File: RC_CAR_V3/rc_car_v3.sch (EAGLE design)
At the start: 45 parts, among them IC1 LIS2DW12TR, IC3 VNH7070BASTR, IC4 BQ34110PWR, J1 282836-2, J2 282836-2, J3 282836-2, Q2 SI2333DDS-T1-GE3, Q3 2N7002-7-F, U1 MCP1703T-3302E/DB

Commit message: PCB
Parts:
- removed IC3: VNH7070BASTR, SamacSys_Parts:VNH7070BASTR
- removed PSOC1: PSOC_5LP, PSoC 5LP:PSOC_5LP
- removed Q3: 2N7002-7-F, SamacSys_Parts:2N7002-7-F
- added C16: 68000-404HLF, SamacSys_Parts:68000-404HLF
- added C17, C18, C19, C20, C21, C22, C23, C24: 0.1uF, SamacSys_Parts:C0603C104K5RAC3121
- added IC2: INA199B3DCKR, SamacSys_Parts:INA199B3DCKR
- added J4: 282836-2, 282836-2:282836-2
- added Q1: 2N7002-7-F, SamacSys_Parts:2N7002-7-F
- added Q5: SQJ912AEP-T2_BE3, SamacSys_Parts:SQJ912AEP-T2_BE3
- added Q7: SI7923DN-T1-E3, SamacSys_Parts:SI7923DN-T1-E3
- C3: value C0603C104K5RAC3121 -> 10uF
- IC4: value BQ34110PWR -> CY8C5888LTI-LP097; device SamacSys_Parts:BQ34110PWR -> SamacSys_Parts:CY8C5888LTI-LP097
- J3: value 282836-2 -> 1-1734742-8; device 282836-2:282836-2 -> SamacSys_Parts:1-1734742-8
- Q2: value SI2333DDS-T1-GE3 -> 2N7002-7-F; device SI2333DDS-T1-GE3:SI2333DDS-T1-GE3 -> SamacSys_Parts:2N7002-7-F
- R10: value ERA-3AED304V -> ERJ-D2DFR022V; device SamacSys_Parts:ERA-3AED304V -> SamacSys_Parts:ERJ-D2DFR022V
- R2, R4: value ERJ-UP3F1000V -> 1k
- R7: value ERJ-3RBD4302V -> 1k; device SamacSys_Parts:ERJ-3RBD4302V -> SamacSys_Parts:ERJ-UP3F1000V
- R8, R9: value ERA-3AED304V -> 1k; device SamacSys_Parts:ERA-3AED304V -> SamacSys_Parts:ERJ-UP3F1000V
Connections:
- removed net BAT: IC4.BAT, R7.2, R8.1
- removed net DIST_1: PSOC1.2.3
- removed net DIST_2: PSOC1.2.2
- removed net DIST_3: PSOC1.2.0
- removed net MOTOR_CURRENT: IC3.CS, R16.1
- removed net N$11: IC3.INB, R15.1
- removed net N$5: C3.1, IC4.REG25
- removed net N$6: Q2.D, R8.2
- removed net N$8: Q2.G, Q3.D, R10.1
- removed net OUTA: IC3.OUTA_1, J3.1
- removed net OUTB: IC3.OUTB_1, J3.2
- removed net PWM: IC3.PWM, R14.2
- removed net PWM1: PSOC1.0.6, R16.2
- removed net SRP: J1.2, R1.1, R4.2
- removed net VEN: IC4.VEN/GPIO, Q3.G
- new net D1: J4.1, Q5.D1_1, Q5.D1_2, Q5.D1_3, Q7.D1_1, Q7.D1_2
- new net D2: J4.2, Q5.D2_1, Q5.D2_2, Q5.D2_3, Q7.D2_1, Q7.D2_2
- new net FWD: Q1.D, Q7.G2, R14.1
- new net IMOTOR: C24.1, IC4.P0[3]_(GPIO,_OPAMP0-,_EXTREF0), R9.1
- new net ISENSE: IC2.OUT, IC4.(OPAMP3-,_EXTREF1,_GPIO)_P3[2]
- new net N$16: C21.2, IC4.(NTRST,_GPIO)_P1[5]
- new net N$21: J3.6, J3.8
- new net RVRS: Q2.D, Q7.G1, R13.1
- new net SRC: Q5.S1, Q5.S2, R10.2, R9.2
- new net SWDCK: IC4.(TCK,_SWDCK,_GPIO)_P1[1], J3.2
- new net SWDIO: IC4.(TMS,_SWDIO,_GPIO)_P1[0], J3.3
- new net VBAT: C3.1, IC4.(OPAMP1+,_GPIO)_P3[5], R2.2, R7.1
- new net XRES: IC4.!XRES, J3.4
- net 0: now also C16.3, C16.4, C17.1, C18.2, C19.1, C20.1, C21.1, C22.2, C23.2, C24.2, IC2.GND, IC2.REF, IC4.EP, IC4.VBAT, IC4.VBOOST, IC4.VSSB, IC4.VSSD_1, IC4.VSSD_2, J1.2, J2.2, Q1.S, Q2.S, R10.1, R2.1; no longer IC3.GNDA_1, IC3.GNDA_2, IC3.GNDB_2, IC4.VSS, PSOC1.GND, PSOC1.GND_3, Q3.S, R1.2, R2.2, R7.1
- net 3.3V: now also IC2.V+, R4.2, R8.2; no longer IC4.REGIN, R3.2, R5.2
- net CTS: now also IC4.(I2C0:_SCL,_SIO)_P12[4]; no longer PSOC1.12.4
- net CTS_JETSON: now also IC4.VDDIO0; no longer PSOC1.2.7
- net ECHO_1: now also IC4.P2[3]_(GPIO,_TRACECLK)
- net ECHO_2: now also IC4.P2[2]_(GPIO)
- net ECHO_3: now also IC4.P2[0]_(GPIO)
- net FORWARD: now also IC4.P0[1]_(GPIO,_OPAMP0OUT), R15.2, R3.2; no longer PSOC1.1.7, R13.2
- net N$10: now also C17.2, C18.1, IC4.VCCD_1, IC4.VCCD_2; no longer IC3.INA, R13.1
- net N$13: now also Q1.G, R16.1; no longer J2.2
- net N$2: now also Q5.G1, R3.1; no longer R10.2, R9.1
- net N$3: now also IC2.IN+, J1.1, R1.1; no longer IC4.SRN, R2.1
- net N$4: now also Q2.G, R15.1; no longer IC4.SRP, R4.1
- net N$7: now also Q5.G2, R5.1; no longer PSOC1.1.6, R14.1
- net REVERSE: now also IC4.P0[7]_(GPIO,_IDAC2), R16.2, R5.2; no longer PSOC1.0.7, R15.2
- net RTS: now also IC4.(I2C0:_SDA,_SIO)_P12[5]; no longer PSOC1.12.5
- net RTS_JETSON: now also IC4.P0[5]_(GPIO,_OPAMP2-); no longer PSOC1.2.6
- net RX: now also IC4.(SIO)_P12[6]; no longer PSOC1.12.2
- net RX_JETSON: now also IC4.P12[3]_(SIO); no longer PSOC1.12.6
- net SCL: now also IC4.P12[0]_(SIO,_12C1:_SCL), R8.1; no longer IC4.SCL, PSOC1.12.0_SCL, R3.1
- net SDA: now also IC4.P12[1]_(SIO,_I2C1:_SDA), R4.1; no longer IC4.SDA, PSOC1.12.1_SDA, R5.1
- net SERVO: now also C16.2, IC4.P2[5]_(GPIO,_TRACEDATA[1]); no longer PSOC1.2.5
- net SPEED: now also IC4.P15[4]_(GPIO); no longer PSOC1.15.4
- net TRIG: now also IC4.P2[4]_(GPIO,_TRACEDATA[0]); no longer PSOC1.2.4
- net TX: now also IC4.(SIO)_P12[7]; no longer PSOC1.12.3
- net TX_JETSON: now also IC4.P12[2]_(SIO); no longer PSOC1.12.7
- net VBUS: now also C16.1, IC2.IN-, Q7.S1, Q7.S2, R1.2, R13.2, R14.2, R7.2; no longer IC3.VCC_1, IC3.VCC_2, IC3.VCC_3, J1.1, Q2.S, R9.2
- net VDD: now also C19.2, C20.2, C22.1, C23.1, IC4.VDDD_1, IC4.VDDD_2, IC4.VDDIO1, IC4.VDDIO2, IC4.VDDIO3; no longer PSOC1.VDD, PSOC1.VDD_2
- net VSENSE: now also IC4.(OPAMP1-,_GPIO)_P3[4]
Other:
- moved on the sheet: C3, R1, R10

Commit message: Added more connections
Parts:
- added C25, C26: 0.1uF, SamacSys_Parts:C0603C104K5RAC3121
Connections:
- new net N$6: C25.2, IC4.VCCA
- net 0: now also C25.1, C26.1, IC4.VSSA, IC4.VSSD_3
- net VDD: now also C26.2, IC4.VDDA
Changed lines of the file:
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@@
 <?xml version="1.0" encoding="utf-8"?>
 <!DOCTYPE eagle SYSTEM "eagle.dtd">
-<eagle version="9.6.2">
+<eagle version="9.3.2">
 <drawing>
 <settings>
@@
 <part name="C24" library="SamacSys_Parts" deviceset="C0603C104K5RAC3121" device="" value="0.1uF"/>
 <part name="X_39" library="ngspice-simulation" library_urn="urn:adsk.eagle:library:527439" deviceset="GND" device=""/>
+<part name="X_40" library="ngspice-simulation" library_urn="urn:adsk.eagle:library:527439" deviceset="GND" device=""/>
+<part name="C25" library="SamacSys_Parts" deviceset="C0603C104K5RAC3121" device="" value="0.1uF"/>
+<part name="X_41" library="ngspice-simulation" library_urn="urn:adsk.eagle:library:527439" deviceset="GND" device=""/>
+<part name="C26" library="SamacSys_Parts" deviceset="C0603C104K5RAC3121" device="" value="0.1uF"/>
+<part name="X_42" library="ngspice-simulation" library_urn="urn:adsk.eagle:library:527439" deviceset="GND" device=""/>
 </parts>
 <sheets>
@@
 <attribute name="VALUE" x="105.41" y="-25.4" size="1.778" layer="96" align="center-left"/>
 </instance>
-<instance part="R4" gate="G$1" x="147.32" y="-106.68" smashed="yes" rot="R90"/>
-<instance part="R8" gate="G$1" x="157.48" y="-106.68" smashed="yes" rot="R90"/>
+<instance part="R4" gate="G$1" x="162.56" y="-106.68" smashed="yes" rot="R90"/>
+<instance part="R8" gate="G$1" x="172.72" y="-106.68" smashed="yes" rot="R90"/>
 <instance part="J4" gate="G$1" x="411.48" y="-162.56" smashed="yes" rot="MR0">
 <attribute name="NAME" x="412.752359375" y="-156.707159375" size="1.017890625" layer="95" rot="MR0"/>
@@
 </instance>
 <instance part="X_39" gate="G$1" x="353.06" y="-203.2" smashed="yes"/>
+<instance part="X_40" gate="G$1" x="134.62" y="-91.44" smashed="yes" rot="R90"/>
+<instance part="C25" gate="G$1" x="132.08" y="-99.06" smashed="yes" rot="R180">
+<attribute name="NAME" x="128.27" y="-102.87" size="1.778" layer="95" rot="R180" align="center-left"/>
+<attribute name="VALUE" x="128.27" y="-95.25" size="1.778" layer="96" rot="R180" align="center-left"/>
+</instance>
+<instance part="X_41" gate="G$1" x="134.62" y="-99.06" smashed="yes" rot="R90"/>
+<instance part="C26" gate="G$1" x="149.86" y="-96.52" smashed="yes" rot="R90">
+<attribute name="NAME" x="146.05" y="-92.71" size="1.778" layer="95" rot="R90" align="center-left"/>
+<attribute name="VALUE" x="153.67" y="-92.71" size="1.778" layer="96" rot="R90" align="center-left"/>
+</instance>
+<instance part="X_42" gate="G$1" x="149.86" y="-99.06" smashed="yes"/>
 </instances>
 <busses>
@@
 </segment>
 <segment>
-<wire x1="147.32" y1="-88.9" x2="147.32" y2="-81.28" width="0.1524" layer="91"/>
-<wire x1="147.32" y1="-81.28" x2="157.48" y2="-81.28" width="0.1524" layer="91"/>
-<wire x1="157.48" y1="-81.28" x2="157.48" y2="-88.9" width="0.1524" layer="91"/>
-<label x="152.4" y="-78.74" size="1.778" layer="95"/>
+<wire x1="162.56" y1="-88.9" x2="162.56" y2="-81.28" width="0.1524" layer="91"/>
+<wire x1="162.56" y1="-81.28" x2="172.72" y2="-81.28" width="0.1524" layer="91"/>
+<wire x1="172.72" y1="-81.28" x2="172.72" y2="-88.9" width="0.1524" layer="91"/>
+<label x="167.64" y="-78.74" size="1.778" layer="95"/>
 <pinref part="R4" gate="G$1" pin="2"/>
 <pinref part="R8" gate="G$1" pin="2"/>
@@
 <pinref part="X_39" gate="G$1" pin="0"/>
 </segment>
+<segment>
+<pinref part="X_40" gate="G$1" pin="0"/>
+<pinref part="IC4" gate="G$1" pin="VSSD_3"/>
+<wire x1="134.62" y1="-91.44" x2="119.38" y2="-91.44" width="0.1524" layer="91"/>
+<pinref part="IC4" gate="G$1" pin="VSSA"/>
+<wire x1="119.38" y1="-91.44" x2="109.22" y2="-91.44" width="0.1524" layer="91"/>
+<wire x1="109.22" y1="-96.52" x2="119.38" y2="-96.52" width="0.1524" layer="91"/>
+<wire x1="119.38" y1="-96.52" x2="119.38" y2="-91.44" width="0.1524" layer="91"/>
+<junction x="119.38" y="-91.44"/>
+</segment>
+<segment>
+<pinref part="C25" gate="G$1" pin="1"/>
+<pinref part="X_41" gate="G$1" pin="0"/>
+<wire x1="132.08" y1="-99.06" x2="134.62" y2="-99.06" width="0.1524" layer="91"/>
+</segment>
+<segment>
+<pinref part="C26" gate="G$1" pin="1"/>
+<pinref part="X_42" gate="G$1" pin="0"/>
+<wire x1="149.86" y1="-96.52" x2="149.86" y2="-99.06" width="0.1524" layer="91"/>
+</segment>
 </net>
 <net name="SCL" class="0">
@@
 <pinref part="IC4" gate="G$1" pin="P12[0]_(SIO,_12C1:_SCL)"/>
 <pinref part="R8" gate="G$1" pin="1"/>
-<wire x1="109.22" y1="-109.22" x2="157.48" y2="-109.22" width="0.1524" layer="91"/>
-<wire x1="157.48" y1="-109.22" x2="157.48" y2="-106.68" width="0.1524" layer="91"/>
-<label x="160.02" y="-109.22" size="1.778" layer="95"/>
+<wire x1="109.22" y1="-109.22" x2="172.72" y2="-109.22" width="0.1524" layer="91"/>
+<wire x1="172.72" y1="-109.22" x2="172.72" y2="-106.68" width="0.1524" layer="91"/>
+<label x="175.26" y="-109.22" size="1.778" layer="95"/>
 </segment>
 </net>
@@
 <pinref part="R4" gate="G$1" pin="1"/>
 <pinref part="IC4" gate="G$1" pin="P12[1]_(SIO,_I2C1:_SDA)"/>
-<wire x1="147.32" y1="-106.68" x2="109.22" y2="-106.68" width="0.1524" layer="91"/>
+<wire x1="162.56" y1="-106.68" x2="109.22" y2="-106.68" width="0.1524" layer="91"/>
 <label x="139.7" y="-104.14" size="1.778" layer="95"/>
 </segment>
@@
 <junction x="7.62" y="-167.64"/>
 </segment>
+<segment>
+<pinref part="IC4" gate="G$1" pin="VDDA"/>
+<wire x1="109.22" y1="-93.98" x2="142.24" y2="-93.98" width="0.1524" layer="91"/>
+<wire x1="142.24" y1="-93.98" x2="142.24" y2="-83.82" width="0.1524" layer="91"/>
+<pinref part="C26" gate="G$1" pin="2"/>
+<wire x1="142.24" y1="-83.82" x2="149.86" y2="-83.82" width="0.1524" layer="91"/>
+<label x="142.24" y="-83.82" size="1.778" layer="95"/>
+</segment>
 </net>
 <net name="N$9" class="0">
@@
 </segment>
 </net>
+<net name="N$6" class="0">
+<segment>
+<pinref part="C25" gate="G$1" pin="2"/>
+<wire x1="119.38" y1="-99.06" x2="109.22" y2="-99.06" width="0.1524" layer="91"/>
+<pinref part="IC4" gate="G$1" pin="VCCA"/>
+</segment>
+</net>

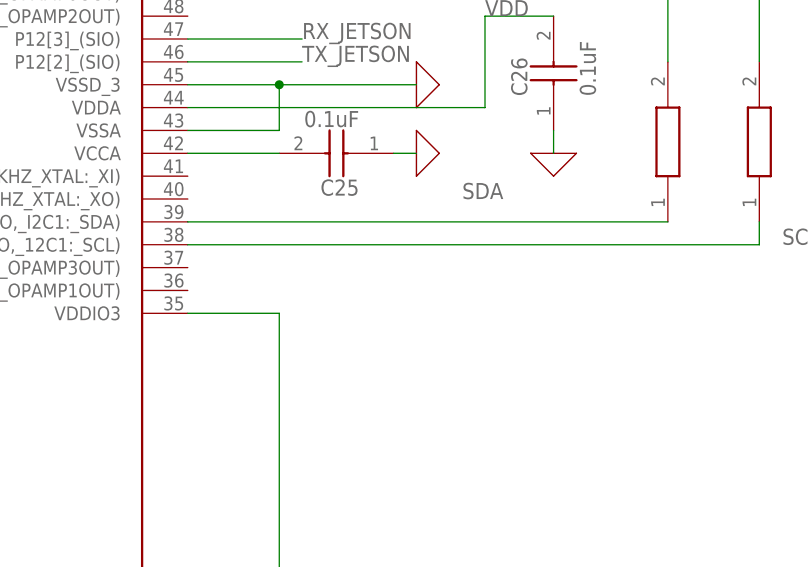
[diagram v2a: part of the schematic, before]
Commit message: Added ground planes
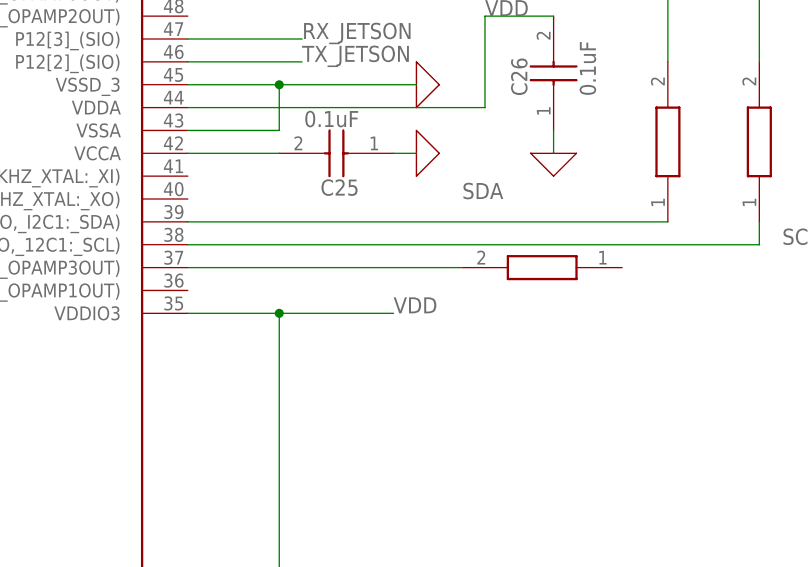
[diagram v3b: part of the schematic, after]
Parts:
- added R18: 1k, SamacSys_Parts:ERJ-UP3F1000V
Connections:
- new net N$5: IC4.P3[7]_(GPIO,_OPAMP3OUT), R18.2
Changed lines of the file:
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@@
 <?xml version="1.0" encoding="utf-8"?>
 <!DOCTYPE eagle SYSTEM "eagle.dtd">
-<eagle version="9.3.2">
+<eagle version="9.6.2">
 <drawing>
 <settings>
@@
 <part name="C26" library="SamacSys_Parts" deviceset="C0603C104K5RAC3121" device="" value="0.1uF"/>
 <part name="X_42" library="ngspice-simulation" library_urn="urn:adsk.eagle:library:527439" deviceset="GND" device=""/>
+<part name="R18" library="SamacSys_Parts" deviceset="ERJ-UP3F1000V" device="" value="1k"/>
 </parts>
 <sheets>
@@
 </instance>
 <instance part="X_42" gate="G$1" x="149.86" y="-99.06" smashed="yes"/>
+<instance part="R18" gate="G$1" x="157.48" y="-111.76" smashed="yes" rot="R180"/>
 </instances>
 <busses>
@@
 <wire x1="7.62" y1="-116.84" x2="7.62" y2="-167.64" width="0.1524" layer="91"/>
 <junction x="7.62" y="-167.64"/>
+<wire x1="119.38" y1="-116.84" x2="132.08" y2="-116.84" width="0.1524" layer="91"/>
+<junction x="119.38" y="-116.84"/>
+<label x="132.08" y="-116.84" size="1.778" layer="95"/>
 </segment>
 <segment>
@@
 </segment>
 </net>
+<net name="N$5" class="0">
+<segment>
+<pinref part="IC4" gate="G$1" pin="P3[7]_(GPIO,_OPAMP3OUT)"/>
+<wire x1="109.22" y1="-111.76" x2="139.7" y2="-111.76" width="0.1524" layer="91"/>
+<pinref part="R18" gate="G$1" pin="2"/>
+</segment>
+</net>
 </nets>
 </sheet>
 </sheets>
+<errors>
+</errors>
 </schematic>
 </drawing>

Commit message: Done
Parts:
- added LED1: LTST-C191TBKT, SamacSys_Parts:LTST-C191TBKT
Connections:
- removed net N$5: IC4.P3[7]_(GPIO,_OPAMP3OUT), R18.2
- new net LED: IC4.(IDAC1,_GPIO)_P3[0], R18.2
- new net N$8: LED1.K, R18.1
- net 5V: now also LED1.A
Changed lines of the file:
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@@
 <part name="X_42" library="ngspice-simulation" library_urn="urn:adsk.eagle:library:527439" deviceset="GND" device=""/>
 <part name="R18" library="SamacSys_Parts" deviceset="ERJ-UP3F1000V" device="" value="1k"/>
+<part name="LED1" library="SamacSys_Parts" deviceset="LTST-C191TBKT" device=""/>
 </parts>
 <sheets>
@@
 </instance>
 <instance part="X_42" gate="G$1" x="149.86" y="-99.06" smashed="yes"/>
-<instance part="R18" gate="G$1" x="157.48" y="-111.76" smashed="yes" rot="R180"/>
+<instance part="R18" gate="G$1" x="134.62" y="-198.12" smashed="yes" rot="R180"/>
+<instance part="LED1" gate="G$1" x="134.62" y="-203.2" smashed="yes" rot="R270">
+<attribute name="NAME" x="143.51" y="-215.9" size="1.778" layer="95" rot="R270"/>
+<attribute name="VALUE" x="140.97" y="-215.9" size="1.778" layer="96" rot="R270"/>
+</instance>
 </instances>
 <busses>
@@
 <wire x1="396.24" y1="-93.98" x2="391.16" y2="-93.98" width="0.1524" layer="91"/>
 <label x="373.38" y="-93.98" size="1.778" layer="95"/>
+</segment>
+<segment>
+<pinref part="LED1" gate="G$1" pin="A"/>
+<wire x1="134.62" y1="-218.44" x2="134.62" y2="-226.06" width="0.1524" layer="91"/>
+<label x="132.08" y="-228.6" size="1.778" layer="95"/>
 </segment>
 </net>
@@
 </segment>
 </net>
-<net name="N$5" class="0">
-<segment>
-<pinref part="IC4" gate="G$1" pin="P3[7]_(GPIO,_OPAMP3OUT)"/>
-<wire x1="109.22" y1="-111.76" x2="139.7" y2="-111.76" width="0.1524" layer="91"/>
+<net name="N$8" class="0">
+<segment>
+<pinref part="LED1" gate="G$1" pin="K"/>
+<pinref part="R18" gate="G$1" pin="1"/>
+<wire x1="134.62" y1="-203.2" x2="134.62" y2="-198.12" width="0.1524" layer="91"/>
+</segment>
+</net>
+<net name="LED" class="0">
+<segment>
 <pinref part="R18" gate="G$1" pin="2"/>
-</segment>
-</net>
+<wire x1="116.84" y1="-198.12" x2="106.68" y2="-198.12" width="0.1524" layer="91"/>
+<label x="101.6" y="-198.12" size="1.778" layer="95"/>
+</segment>
+<segment>
+<pinref part="IC4" gate="G$1" pin="(IDAC1,_GPIO)_P3[0]"/>
+<wire x1="66.04" y1="-165.1" x2="66.04" y2="-172.72" width="0.1524" layer="91"/>
+<label x="66.04" y="-180.34" size="1.778" layer="95" rot="R90"/>
+</segment>
+</net>

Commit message: Cganges
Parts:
- removed Q1, Q2: 2N7002-7-F, SamacSys_Parts:2N7002-7-F
- removed Q5: SQJ912AEP-T2_BE3, SamacSys_Parts:SQJ912AEP-T2_BE3
- removed Q7: SI7923DN-T1-E3, SamacSys_Parts:SI7923DN-T1-E3
- removed R10: ERJ-D2DFR022V, SamacSys_Parts:ERJ-D2DFR022V
- removed R13, R14, R15, R16, R3, R5, R9: 1k, SamacSys_Parts:ERJ-UP3F1000V
- added IC3: MC33HB2000AES, SamacSys_Parts:MC33HB2000AES
- C24: value 0.1uF -> 1uF
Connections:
- removed net FWD: Q1.D, Q7.G2, R14.1
- removed net N$13: Q1.G, R16.1
- removed net N$2: Q5.G1, R3.1
- removed net N$4: Q2.G, R15.1
- removed net RVRS: Q2.D, Q7.G1, R13.1
- removed net SRC: Q5.S1, Q5.S2, R10.2, R9.2
- new net CS: IC3.CS_B, IC4.P2[1]_(GPIO)
- new net DISABLE: IC3.DIS, IC4.(GPIO)_P1[6]
- new net ENABLE: IC3.ENBL, IC4.(GPIO)_P1[7]
- new net MISO: IC3.MISO, IC4.(TDI,_GPIO)_P1[4]
- new net MOSI: IC3.MOSI, IC4.(CONFIGURABLE_!XRES,_GPIO)_P1[2]
- new net N$12: IC3.PGND_1, IC3.PGND_2, IC3.PGND_3, IC3.PGND_4
- new net N$18: C24.2, IC3.CCP
- new net SCLK: IC3.SCLK, IC4.(TDO,_SWV,_GPIO)_P1[3]
- net 0: now also IC3.AGND_1, IC3.AGND_2, IC3.DGND, IC3.PGND_5; no longer C24.2, Q1.S, Q2.S, R10.1
- net D1: now also IC3.OUT1_1, IC3.OUT1_2; no longer Q5.D1_1, Q5.D1_2, Q5.D1_3, Q7.D1_1, Q7.D1_2
- net D2: now also IC3.OUT2_1, IC3.OUT2_2; no longer Q5.D2_1, Q5.D2_2, Q5.D2_3, Q7.D2_1, Q7.D2_2
- net FORWARD: now also IC3.IN2; no longer R15.2, R3.2
- net IMOTOR: now also IC3.CFB; no longer C24.1, R9.1
- net N$7: now also IC3.AGND_10, IC3.AGND_11, IC3.AGND_3, IC3.AGND_4, IC3.AGND_5, IC3.AGND_6, IC3.AGND_7, IC3.AGND_8, IC3.AGND_9; no longer Q5.G2, R5.1
- net REVERSE: now also IC3.IN1; no longer R16.2, R5.2
- net VBUS: now also C24.1, IC3.VPWR_1, IC3.VPWR_2, IC3.VPWR_3, IC3.VPWR_4; no longer Q7.S1, Q7.S2, R13.2, R14.2
- net VDD: now also IC3.VDDQ
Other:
- moved on the sheet: C24

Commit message: Changes
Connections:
- removed net N$12: IC3.PGND_1, IC3.PGND_2, IC3.PGND_3, IC3.PGND_4
- removed net N$7: IC3.AGND_10, IC3.AGND_11, IC3.AGND_3, IC3.AGND_4, IC3.AGND_5, IC3.AGND_6, IC3.AGND_7, IC3.AGND_8, IC3.AGND_9
- net 0: now also IC3.AGND_10, IC3.AGND_11, IC3.AGND_3, IC3.AGND_4, IC3.AGND_5, IC3.AGND_6, IC3.AGND_7, IC3.AGND_8, IC3.AGND_9, IC3.PGND_1, IC3.PGND_2, IC3.PGND_3, IC3.PGND_4
